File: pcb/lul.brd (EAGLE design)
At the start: 90 x 96 mm, 79 parts, among them IC1 STM32F072C8T6, IC2 REG1117, IC3 74LVC1G125DBV, U1 UG-2864HSWEG01, X1 USB-MICROB

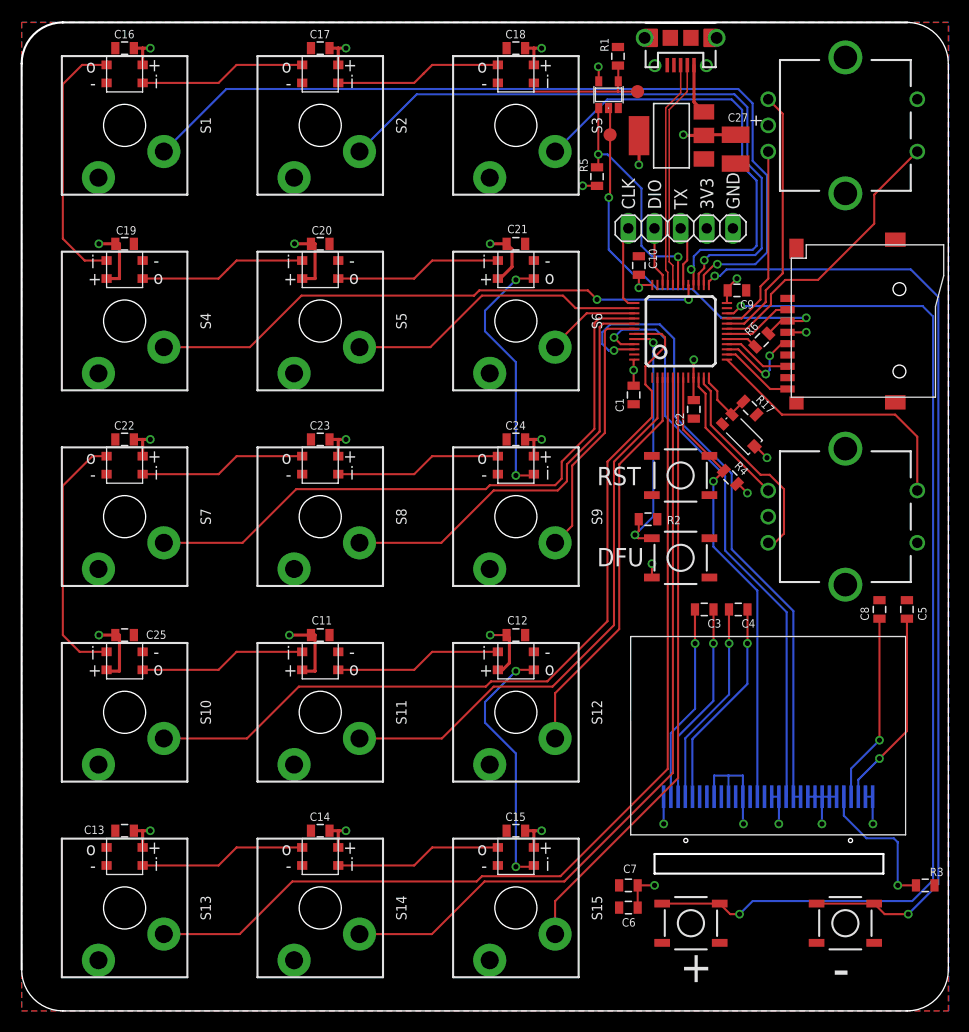
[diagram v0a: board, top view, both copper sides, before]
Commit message: adjusted position of led cap
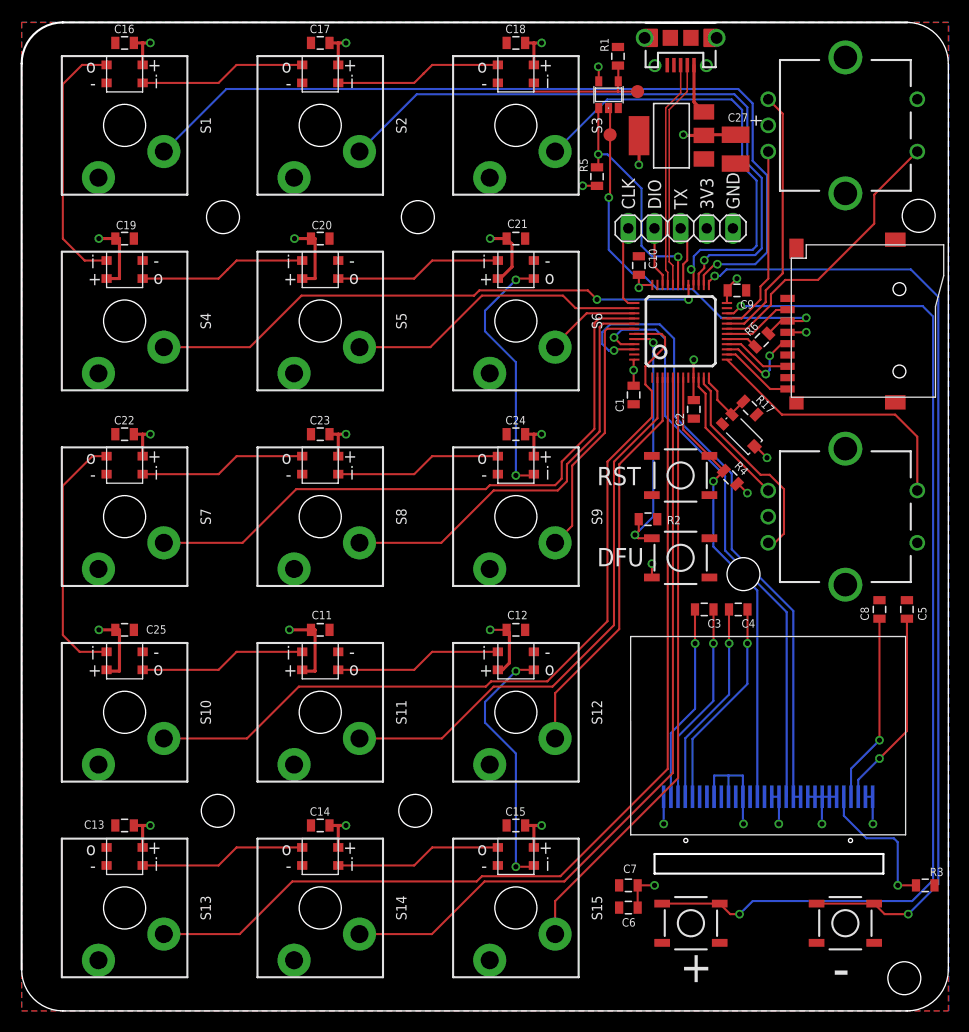
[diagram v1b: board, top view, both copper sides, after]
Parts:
- added U$10, U$11, U$12, U$13, U$14, U$7, U$9: M3_MOUNTING_HOLE, clock:M3_MOUNTING_HOLE_PACK
- moved C11 0.51 mm to (29.0, 37.0)
- moved C12 0.51 mm to (48.0, 37.0)
- moved C22 0.51 mm to (10.0, 56.0)
- moved C23 0.51 mm to (29.0, 56.0)
- moved C24 0.51 mm to (48.0, 56.0)
- moved C25 0.51 mm to (10.0, 37.0)
- moved C13 0.51 mm to (10.0, 18.0)
- moved C14 0.51 mm to (29.0, 18.0)
- moved C15 0.51 mm to (48.0, 18.0)
- moved C16 0.51 mm to (10.0, 94.0)
- moved C17 0.51 mm to (29.0, 94.0)
- moved C18 0.51 mm to (48.0, 94.0)
- moved C19 0.51 mm to (10.0, 75.0)
- moved C20 0.51 mm to (29.0, 75.0)
- moved C21 0.51 mm to (48.0, 75.0)
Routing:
- net +3V3: track 101.0 -> 108.7 mm

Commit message: v1
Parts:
- added U$15, U$16: M3_MOUNTING_HOLE, clock:M3_MOUNTING_HOLE_PACK
- moved U$10 22.6 mm to (71.0, 93.0)
- moved U$9 22.0 mm to (87.0, 56.5)
- moved U$14 13.2 mm to (72.5, 3.00)
- moved C5 2.27 mm to (88.0, 40.0), turned to 180 degrees
- moved C8 1.53 mm to (84.5, 40.0), turned to 180 degrees
- moved C3 1.02 mm to (66.3, 40.0)
- moved C4 1.02 mm to (69.6, 40.0)
- moved U$11 0.59 mm to (19.5, 76.5)
- moved U$13 0.59 mm to (38.5, 76.5)
- moved U$7 0.46 mm to (19.5, 19.5)
- moved U$12 0.28 mm to (38.5, 19.5)
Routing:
- net BUTTON2: track 103.6 -> 95.3 mm
- net BUTTON1: track 94.7 -> 87.0 mm
- net N$11: track 19.2 -> 21.6 mm
- net E2_SW: track 26.8 -> 24.7 mm
- net N$12: track 18.4 -> 20.4 mm
- net N$7: track 20.4 -> 21.4 mm
- net N$6: track 20.0 -> 21.0 mm
- net N$5: track 19.6 -> 20.6 mm
- net N$4: track 19.2 -> 20.2 mm
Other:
- outline, holes or cut-outs redrawn

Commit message: started working on board firmware
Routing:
- net N$3: track 14.1 -> 13.6 mm
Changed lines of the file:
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@@
 <layer number="14" name="Route14" color="1" fill="6" visible="no" active="no"/>
 <layer number="15" name="Route15" color="4" fill="6" visible="no" active="no"/>
-<layer number="16" name="Bottom" color="1" fill="1" visible="yes" active="yes"/>
+<layer number="16" name="Bottom" color="1" fill="1" visible="no" active="yes"/>
 <layer number="17" name="Pads" color="2" fill="1" visible="yes" active="yes"/>
 <layer number="18" name="Vias" color="2" fill="1" visible="yes" active="yes"/>
@@
 <layer number="20" name="Dimension" color="15" fill="1" visible="yes" active="yes"/>
 <layer number="21" name="tPlace" color="7" fill="1" visible="yes" active="yes"/>
-<layer number="22" name="bPlace" color="7" fill="1" visible="yes" active="yes"/>
+<layer number="22" name="bPlace" color="7" fill="1" visible="no" active="yes"/>
 <layer number="23" name="tOrigins" color="15" fill="1" visible="yes" active="yes"/>
-<layer number="24" name="bOrigins" color="15" fill="1" visible="yes" active="yes"/>
+<layer number="24" name="bOrigins" color="15" fill="1" visible="no" active="yes"/>
 <layer number="25" name="tNames" color="7" fill="1" visible="yes" active="yes"/>
-<layer number="26" name="bNames" color="7" fill="1" visible="yes" active="yes"/>
-<layer number="27" name="tValues" color="7" fill="1" visible="yes" active="yes"/>
-<layer number="28" name="bValues" color="7" fill="1" visible="yes" active="yes"/>
+<layer number="26" name="bNames" color="7" fill="1" visible="no" active="yes"/>
+<layer number="27" name="tValues" color="7" fill="1" visible="no" active="yes"/>
+<layer number="28" name="bValues" color="7" fill="1" visible="no" active="yes"/>
 <layer number="29" name="tStop" color="7" fill="3" visible="no" active="yes"/>
 <layer number="30" name="bStop" color="7" fill="6" visible="no" active="yes"/>
@@
 <layer number="37" name="tTest" color="7" fill="1" visible="no" active="yes"/>
 <layer number="38" name="bTest" color="7" fill="1" visible="no" active="yes"/>
-<layer number="39" name="tKeepout" color="4" fill="11" visible="no" active="yes"/>
+<layer number="39" name="tKeepout" color="4" fill="11" visible="yes" active="yes"/>
 <layer number="40" name="bKeepout" color="1" fill="11" visible="no" active="yes"/>
-<layer number="41" name="tRestrict" color="4" fill="10" visible="no" active="yes"/>
+<layer number="41" name="tRestrict" color="4" fill="10" visible="yes" active="yes"/>
 <layer number="42" name="bRestrict" color="1" fill="10" visible="no" active="yes"/>
 <layer number="43" name="vRestrict" color="2" fill="10" visible="no" active="yes"/>
 <layer number="44" name="Drills" color="7" fill="1" visible="no" active="yes"/>
-<layer number="45" name="Holes" color="7" fill="1" visible="no" active="yes"/>
-<layer number="46" name="Milling" color="3" fill="1" visible="no" active="yes"/>
+<layer number="45" name="Holes" color="7" fill="1" visible="yes" active="yes"/>
+<layer number="46" name="Milling" color="3" fill="1" visible="yes" active="yes"/>
 <layer number="47" name="Measures" color="7" fill="1" visible="no" active="yes"/>
 <layer number="48" name="Document" color="7" fill="1" visible="no" active="yes"/>
 <layer number="49" name="Reference" color="7" fill="1" visible="no" active="yes"/>
 <layer number="50" name="dxf" color="7" fill="1" visible="no" active="no"/>
-<layer number="51" name="tDocu" color="7" fill="1" visible="no" active="yes"/>
+<layer number="51" name="tDocu" color="7" fill="1" visible="yes" active="yes"/>
 <layer number="52" name="bDocu" color="7" fill="1" visible="no" active="yes"/>
 <layer number="53" name="tGND_GNDA" color="7" fill="9" visible="no" active="no"/>
@@
 <contactref element="U1" pad="26"/>
 <contactref element="R3" pad="2"/>
-<via x="85.09" y="12.192" extent="1-16" drill="0.5"/>
+<via x="85.09" y="13.081" extent="1-16" drill="0.5"/>
 <wire x1="79.85" y1="18.956" x2="82.042" y2="16.764" width="0.2032" layer="16"/>
 <wire x1="82.042" y1="16.764" x2="84.709" y2="16.764" width="0.2032" layer="16"/>
 <wire x1="84.709" y1="16.764" x2="85.09" y2="16.383" width="0.2032" layer="16"/>
-<wire x1="85.09" y1="16.383" x2="85.09" y2="12.192" width="0.2032" layer="16"/>
+<wire x1="85.09" y1="16.383" x2="85.09" y2="13.081" width="0.2032" layer="16"/>
 <wire x1="79.85" y1="20.8" x2="79.85" y2="18.956" width="0.2032" layer="16"/>
-<wire x1="86.857" y1="12.192" x2="85.09" y2="12.192" width="0.2032" layer="1"/>
+<wire x1="86.857" y1="12.192" x2="85.979" y2="12.192" width="0.2032" layer="1"/>
+<wire x1="85.979" y1="12.192" x2="85.09" y2="13.081" width="0.2032" layer="1"/>
 </signal>
 <signal name="N$4">

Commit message: RTOS working start
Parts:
- C3, C4, C6, C7: value 1uF -> 2.2uF
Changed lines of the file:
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@@
 <attribute name="NAME" x="89.535" y="13.9065" size="0.8128" layer="25" rot="R180"/>
 </element>
-<element name="C3" library="clock" package="0805@1" value="1uF" x="66.294" y="40.005" smashed="yes" rot="R180">
+<element name="C3" library="clock" package="0805@1" value="2.2uF" x="66.294" y="40.005" smashed="yes" rot="R180">
 <attribute name="NAME" x="67.945" y="39.0525" size="0.8128" layer="25" rot="R180"/>
 </element>
-<element name="C4" library="clock" package="0805@1" value="1uF" x="69.596" y="40.005" smashed="yes" rot="R180">
+<element name="C4" library="clock" package="0805@1" value="2.2uF" x="69.596" y="40.005" smashed="yes" rot="R180">
 <attribute name="NAME" x="71.247" y="39.0525" size="0.8128" layer="25" rot="R180"/>
 </element>
@@
 <attribute name="NAME" x="88.265" y="38.9255" size="0.8128" layer="25" rot="R180"/>
 </element>
-<element name="C7" library="clock" package="0805@1" value="1uF" x="58.928" y="12.192" smashed="yes">
+<element name="C7" library="clock" package="0805@1" value="2.2uF" x="58.928" y="12.192" smashed="yes">
 <attribute name="NAME" x="57.531" y="13.2715" size="0.8128" layer="25"/>
 </element>
@@
 <attribute name="NAME" x="84.836" y="38.9255" size="0.8128" layer="25" rot="R180"/>
 </element>
-<element name="C6" library="clock" package="0805@1" value="1uF" x="58.928" y="10.033" smashed="yes">
+<element name="C6" library="clock" package="0805@1" value="2.2uF" x="58.928" y="10.033" smashed="yes">
 <attribute name="NAME" x="58.293" y="8.1915" size="0.8128" layer="25"/>
 </element>
